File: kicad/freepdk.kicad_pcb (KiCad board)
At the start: 2 copper layers, 79 x 35.6 mm, 58 parts, among them J1 MiniUSB, J2 SWD, J3 Conn_01x08, J4 Conn_01x08, J5 Conn_01x02, U1 STM32F072C8Tx, U2 XC6206P332MR, U3 MT3608, U4 LM2904DR2G, Y1 8MHz

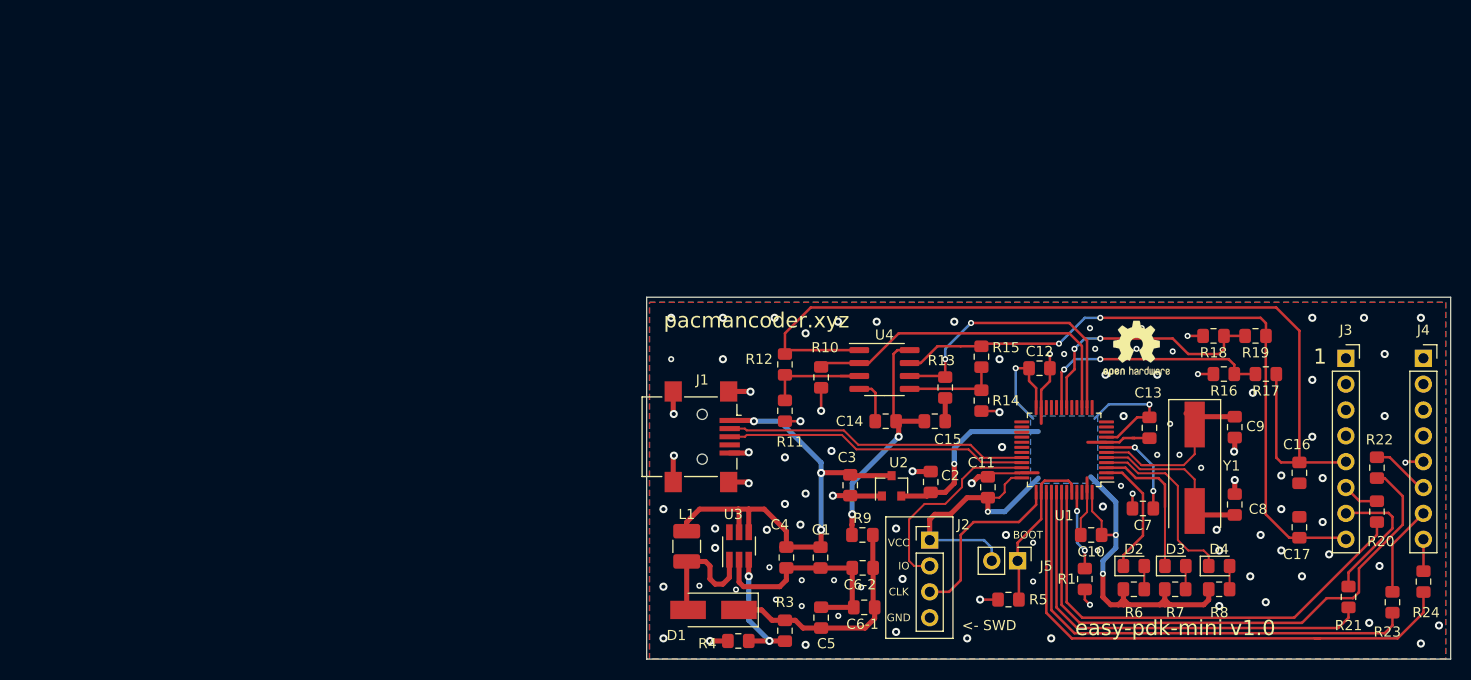
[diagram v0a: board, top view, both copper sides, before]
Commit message: Second revision - Added fuse, improved routing, changed pcb dimentsions
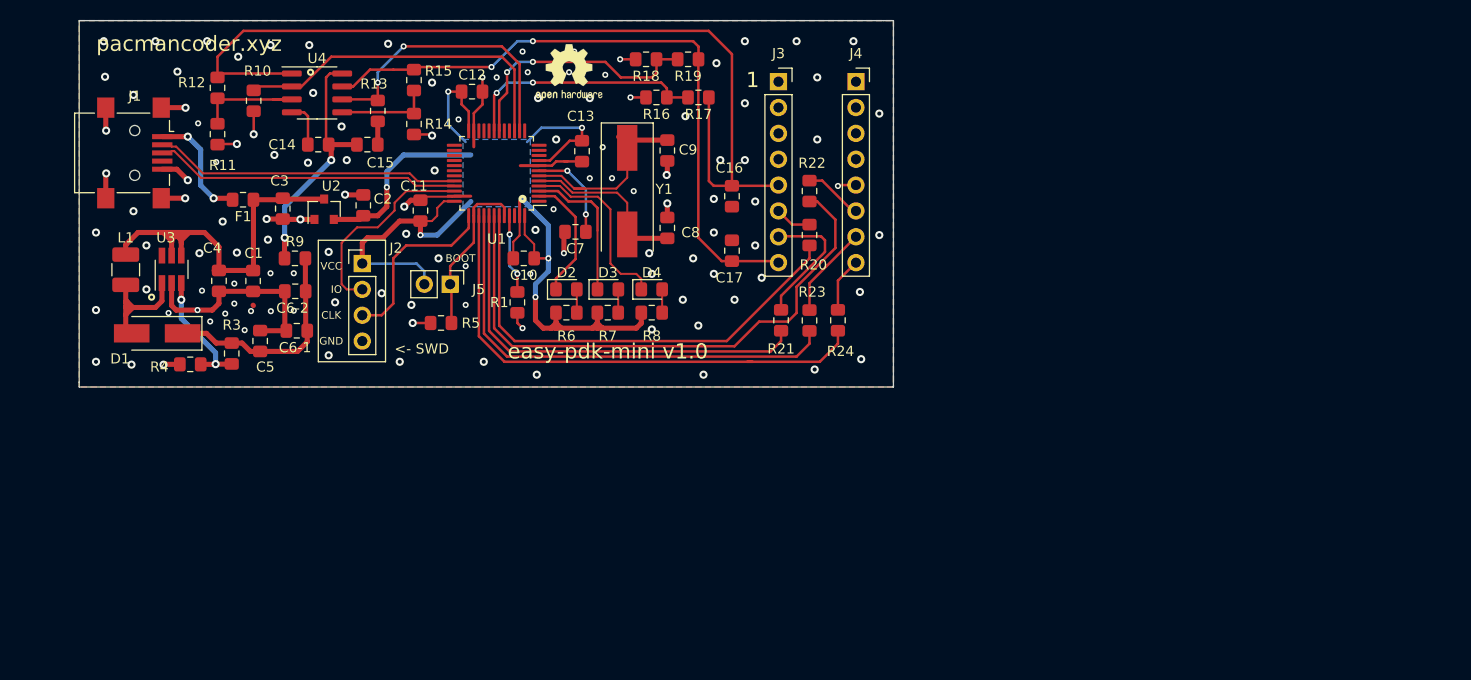
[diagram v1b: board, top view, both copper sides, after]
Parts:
- added F1: 0.5A, Fuse:Fuse_0805_2012Metric_Pad1.15x1.40mm_HandSolder, F.Cu at (79.3, 53.4)
- moved R23 63.6 mm to (135.0, 65.3)
- moved R24 63.0 mm to (137.8, 65.3)
- moved J1 62.3 mm to (68.7, 48.8)
- moved C1 62.0 mm to (80.3, 61.4)
- moved C12 62.0 mm to (101.8, 42.8)
- moved C14 62.0 mm to (86.7, 48.0)
- moved C2 62.0 mm to (91.2, 54.0)
- moved C4 62.0 mm to (77.0, 61.4)
- moved C6-1 62.0 mm to (84.6, 66.3)
- moved C6-2 62.0 mm to (84.5, 62.4)
- moved C7 62.0 mm to (112.0, 56.6)
- moved J2 62.0 mm to (91.1, 59.7)
- moved J4 62.0 mm to (139.6, 41.8)
- moved J5 62.0 mm to (99.7, 61.7)
- moved R13 62.0 mm to (92.6, 44.7)
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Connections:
- J1 pad 1: +5V -> Net-(F1-Pad2)
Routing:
- net Net-(F1-Pad2): track 0.00 -> 11.5 mm, vias 0 -> 2
- net +5V: track 48.2 -> 40.9 mm, vias 3 -> 0
- net /PROG_IPCK_PA3: track 53.5 -> 50.7 mm
- net Net-(J4-Pad8): track 3.14 -> 5.43 mm
- net GND: track 93.1 -> 94.5 mm, vias 102 -> 123
- net /PROG_PA4: track 47.6 -> 46.3 mm
- net +15V: track 23.0 -> 21.9 mm
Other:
- board size 79 x 35.6 mm -> 80 x 36 mm
- board text added: "Mounting places have the same size/distance for all corners"

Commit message: Fixed silkscreen and markings
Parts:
- D2: value LED -> LED1
- D3: value LED -> LED2
- D4: value LED -> LED3
- F1: value 0.5A -> PTC 0.5A 6V
- J3: value Conn_01x08 -> CONN_L
- J4: value Conn_01x08 -> CONN_R
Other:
- board text added: "easy-pdk-mini v1.0.2"
- board text removed: "easy-pdk-mini v1.0"

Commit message: Revision 3 - Applied suggestions from review, prepared gerbers
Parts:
- added G***: LOGO, QR:free-pdk-qr, B.Cu at (103.3, 51.2)
- D2: value LED1 -> LED
- D3: value LED2 -> LED
- D4: value LED3 -> LED
- moved ? 0.52 mm to (111.2, 41.4)
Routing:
- net GND: track 94.5 -> 92.7 mm
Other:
- board text added: "easy-pdk-mini v1.0.3"
- board text added: "free-pdk.github.io"
- board text removed: "easy-pdk-mini v1.0.2"

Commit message: Revision 3 patch: Replaced wrong opamp; Removed logo from BOM
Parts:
- U4: value LM2904DR2G -> LM358DR2G

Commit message: Fixed issue with wrong opamp wiring
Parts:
- moved R10 0.94 mm to (80.4, 44.6)
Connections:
- U4 pad 2: /DAC_VDD -> Net-(R11-Pad1)
- U4 pad 3: Net-(R11-Pad1) -> /DAC_VDD
- U4 pad 5: Net-(R14-Pad1) -> /DAC_VPP
- U4 pad 6: /DAC_VPP -> Net-(R14-Pad1)
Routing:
- net /DAC_VDD: track 33.7 -> 34.8 mm
- net /DAC_VPP: track 28.6 -> 27.7 mm
- net Net-(R14-Pad1): track 9.38 -> 10.1 mm
- net GND: track 92.7 -> 92.2 mm, vias 123 -> 127
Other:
- board text added: "easy-pdk-mini v1.0.4"
- board text removed: "easy-pdk-mini v1.0.3"

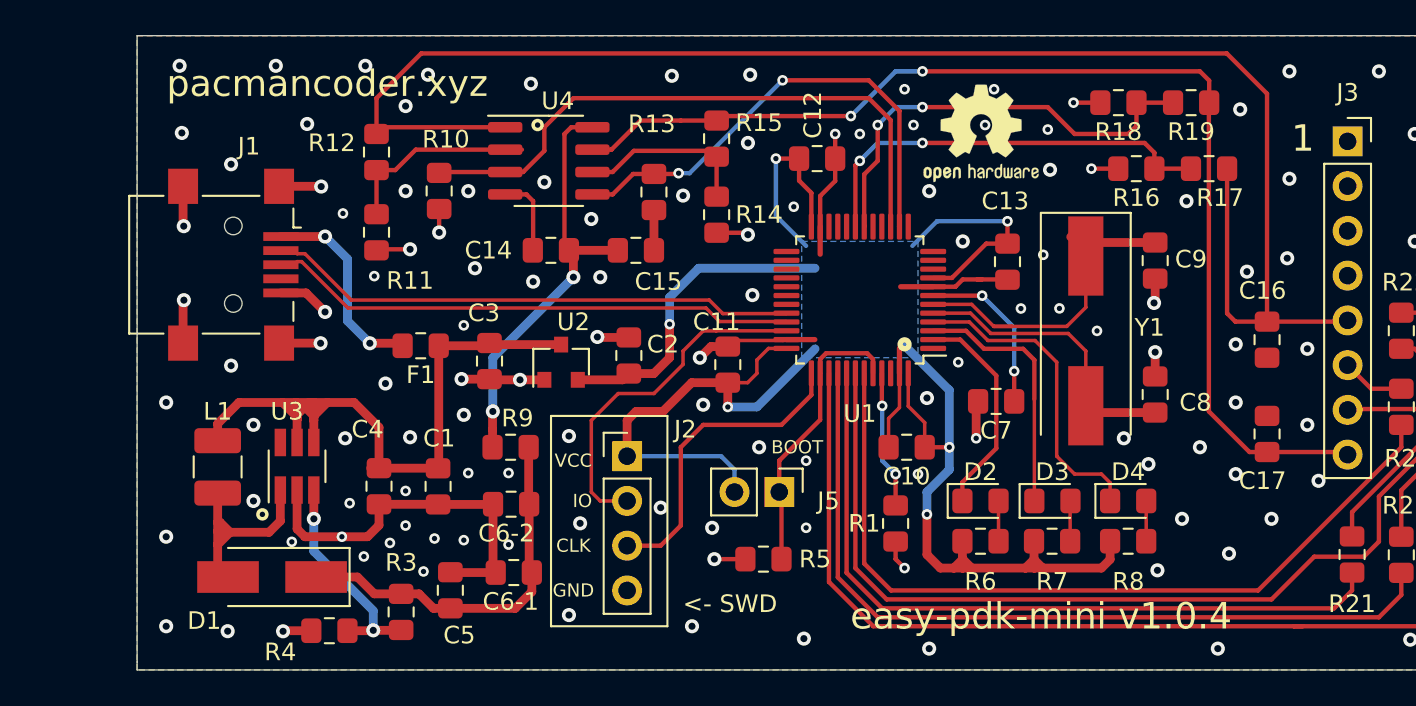
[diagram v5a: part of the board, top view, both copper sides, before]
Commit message: Updated PCB to use USB-B port instead of Mini-usb
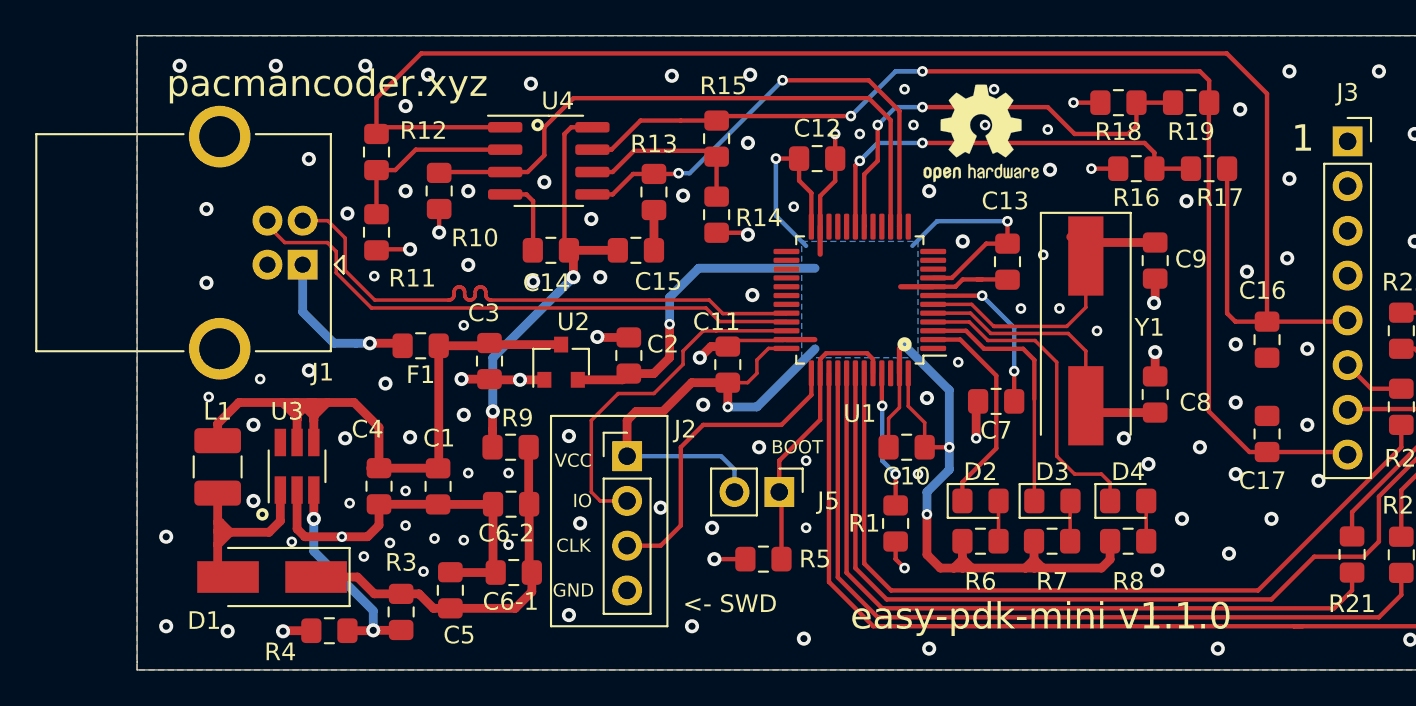
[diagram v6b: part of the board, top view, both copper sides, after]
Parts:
- J1: value MiniUSB -> USB_B; footprint Connector_USB:USB_Mini-B_Lumberg_2486_01_Horizontal -> Connector_USB:USB_B_OST_USB-B1HSxx_Horizontal
- moved J1 3.94 mm to (72.6, 48.8), turned to 180 degrees
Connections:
- J1 pad 4: Net-(J1-Pad4) -> GND
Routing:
- net GND: track 92.2 -> 79.8 mm, vias 127 -> 123
- net /USB_D-: track 30.2 -> 32.7 mm
- net /USB_D+: track 30.2 -> 32.7 mm
- net Net-(F1-Pad2): track 11.5 -> 9.15 mm, vias 2 -> 1
- net Net-(R11-Pad1): track 11.6 -> 10.7 mm
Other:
- board text added: "easy-pdk-mini v1.1.0"
- board text removed: "easy-pdk-mini v1.0.4"

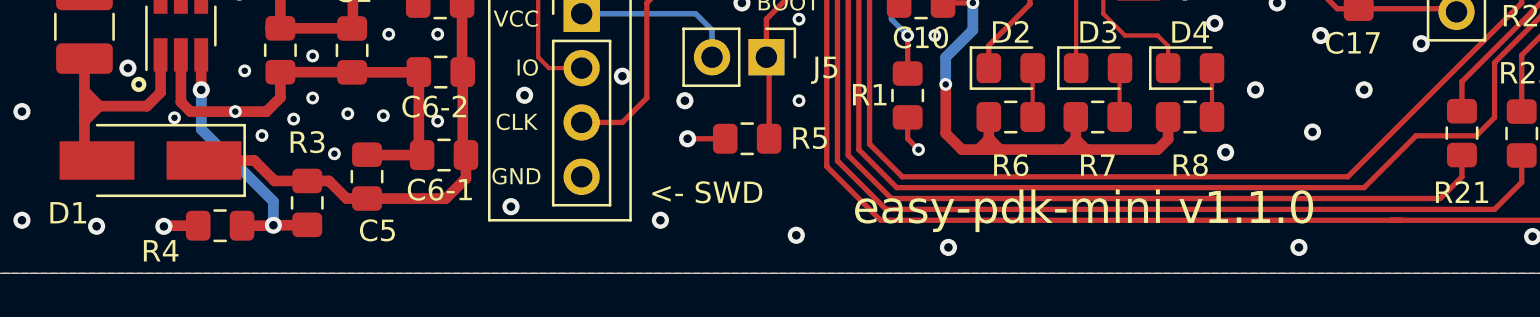
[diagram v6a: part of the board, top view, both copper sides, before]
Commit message: Updated interactive BOM and updated gerbers after minor bugfixes
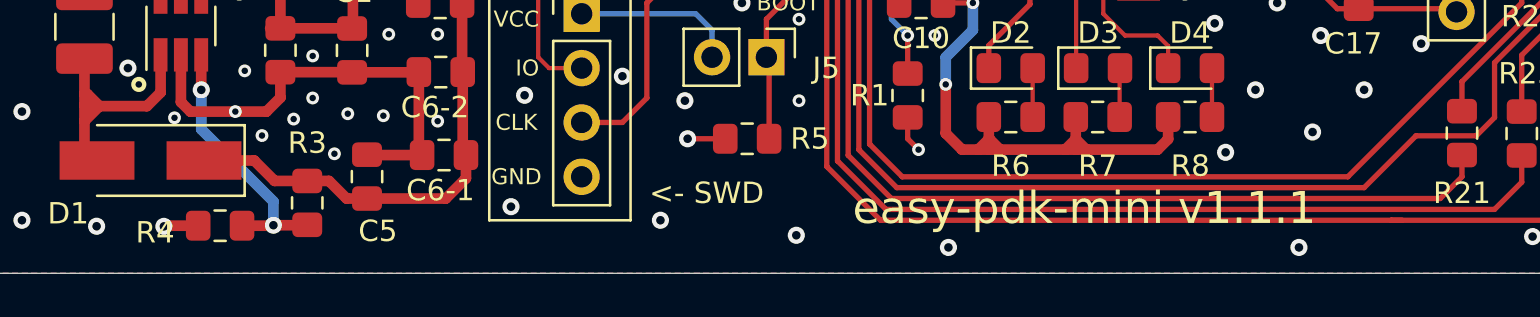
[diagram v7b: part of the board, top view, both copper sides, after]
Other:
- board text added: "easy-pdk-mini v1.1.1"
- board text removed: "easy-pdk-mini v1.1.0"
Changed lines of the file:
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@@
   (general
     (thickness 1.6)
-    (drawings 58)
+    (drawings 61)
     (tracks 684)
     (zones 0)
@@
     (title easy-pdk-mini)
     (date 2020-09-23)
-    (rev 1.1.0)
+    (rev 1.1.1)
     (company "Vladislav Nikonov aka pacmancoder")
     (comment 1 pacmancoder.xyz)
@@
   )
   (layers
-    (0 F.Cu signal)
-    (31 B.Cu signal)
+    (0 F.Cu signal hide)
+    (31 B.Cu signal hide)
     (32 B.Adhes user)
     (33 F.Adhes user)
@@
     (tags "resistor handsolder")
     (attr smd)
-    (fp_text reference R4 (at 2.785 -1.21) (layer F.SilkS)
+    (fp_text reference R4 (at 3.039 -0.321) (layer F.SilkS)
       (effects (font (size 1 1) (thickness 0.15)))
     )
@@
     )
   )
+  (gr_text NC (at 137.033 41.91) (layer B.SilkS)
+    (effects (font (size 1 1) (thickness 0.15)) (justify mirror))
+  )
+  (gr_text NC (at 129.413 41.91) (layer B.SilkS)
+    (effects (font (size 1 1) (thickness 0.15)) (justify mirror))
+  )
+  (gr_text NC (at 129.413 44.45) (layer B.SilkS)
+    (effects (font (size 1 1) (thickness 0.15)) (justify mirror))
+  )
   (gr_poly (pts (xy 65.247 70.822) (xy 63.247 70.822) (xy 63.247 65.822) (xy 65.247 65.822)) (layer Dwgs.User) (width 0.1))
   (gr_line (start 65.247 70.822) (end 65.247 65.822) (layer Dwgs.User) (width 0.15))
@@
     (arrow2b (pts (xy 53.247 71.822) (xy 52.660579 70.695496)))
   )
-  (gr_text free-pdk.github.io (at 77.979 41.723) (layer B.SilkS)
+  (gr_text free-pdk.github.io (at 74.677 38.548) (layer B.SilkS)
     (effects (font (size 1.4 1.4) (thickness 0.2)) (justify mirror))
   )
@@
     (effects (font (size 1 1) (thickness 0.15)))
   )
-  (gr_text "easy-pdk-mini v1.1.0" (at 114.555 68.774) (layer F.SilkS)
+  (gr_text "easy-pdk-mini v1.1.1" (at 114.555 68.774) (layer F.SilkS)
     (effects (font (size 1.5 1.5) (thickness 0.3)))
   )
